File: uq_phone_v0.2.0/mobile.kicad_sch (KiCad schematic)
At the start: 29 parts, among them J10 513382474, J11 513382474, J12 20279-001E-03, J4 20279-001E-03, J5 20279-001E-03, U4 RC7620_1104626

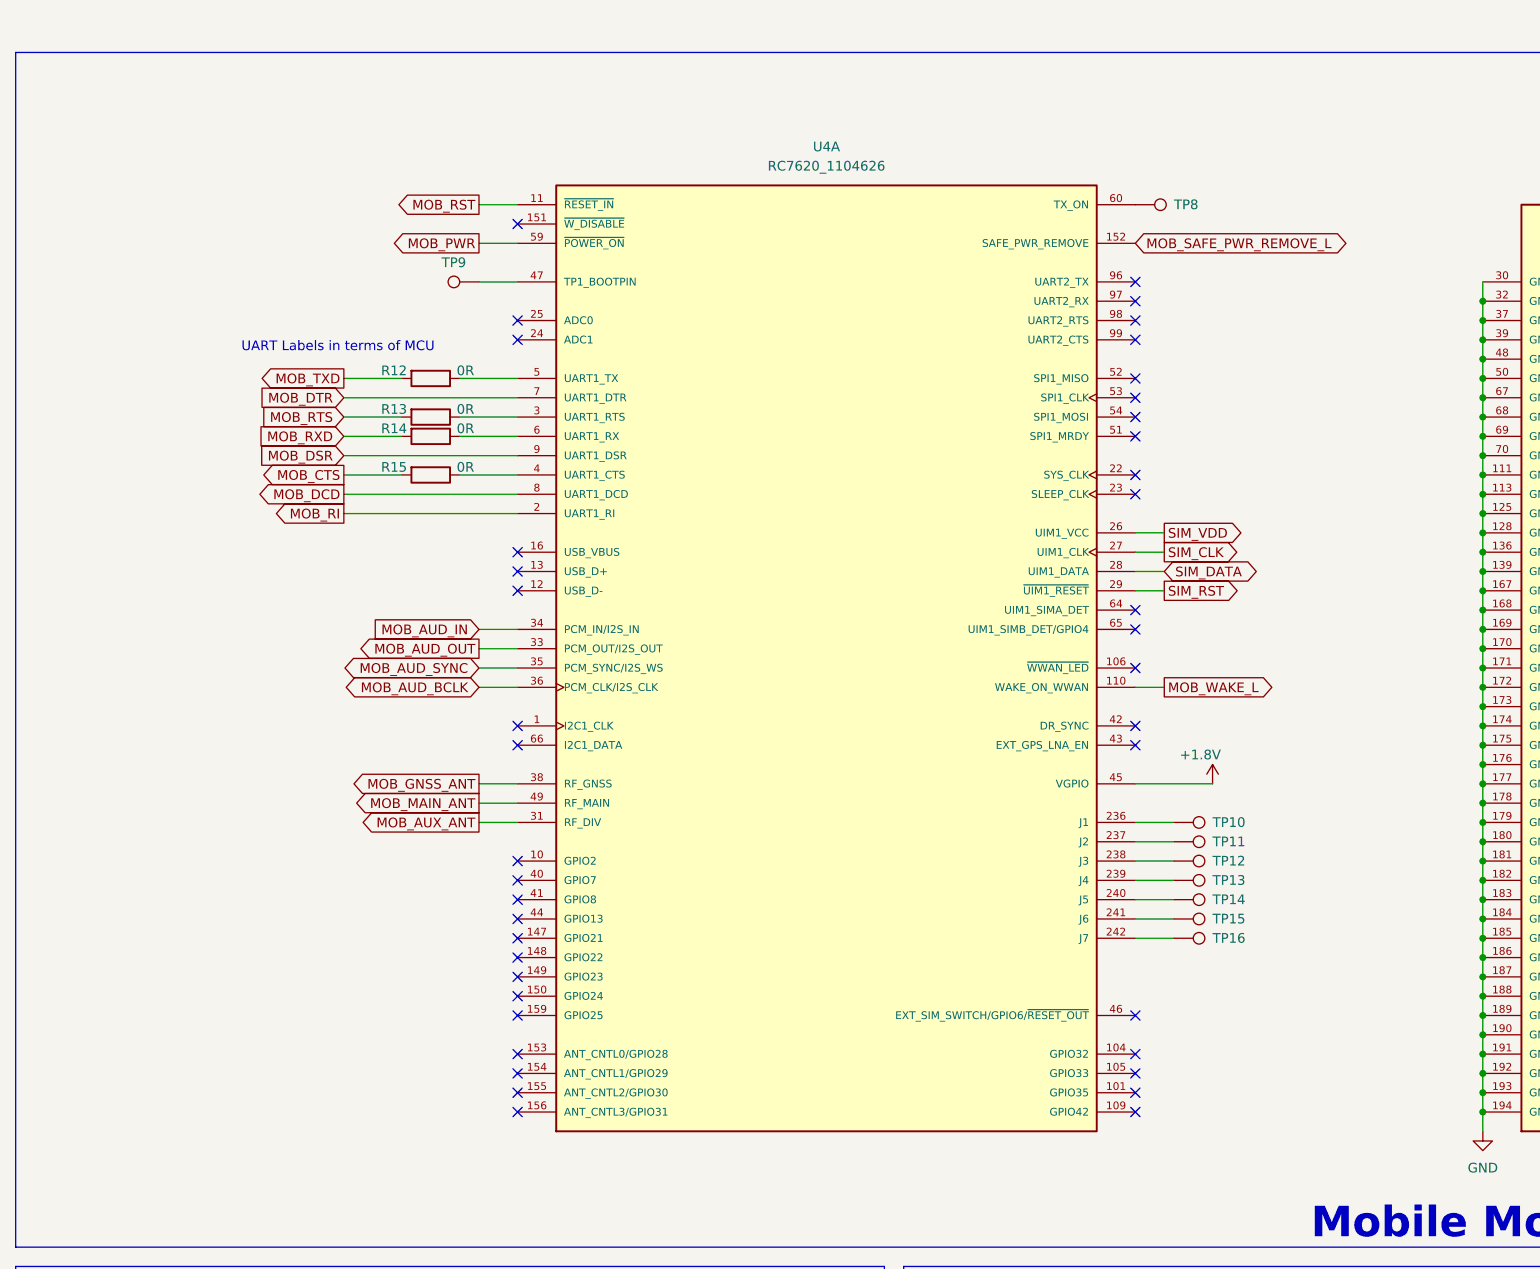
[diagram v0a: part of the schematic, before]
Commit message: Add shared tray detect for MCU and RC7620 SIM detection
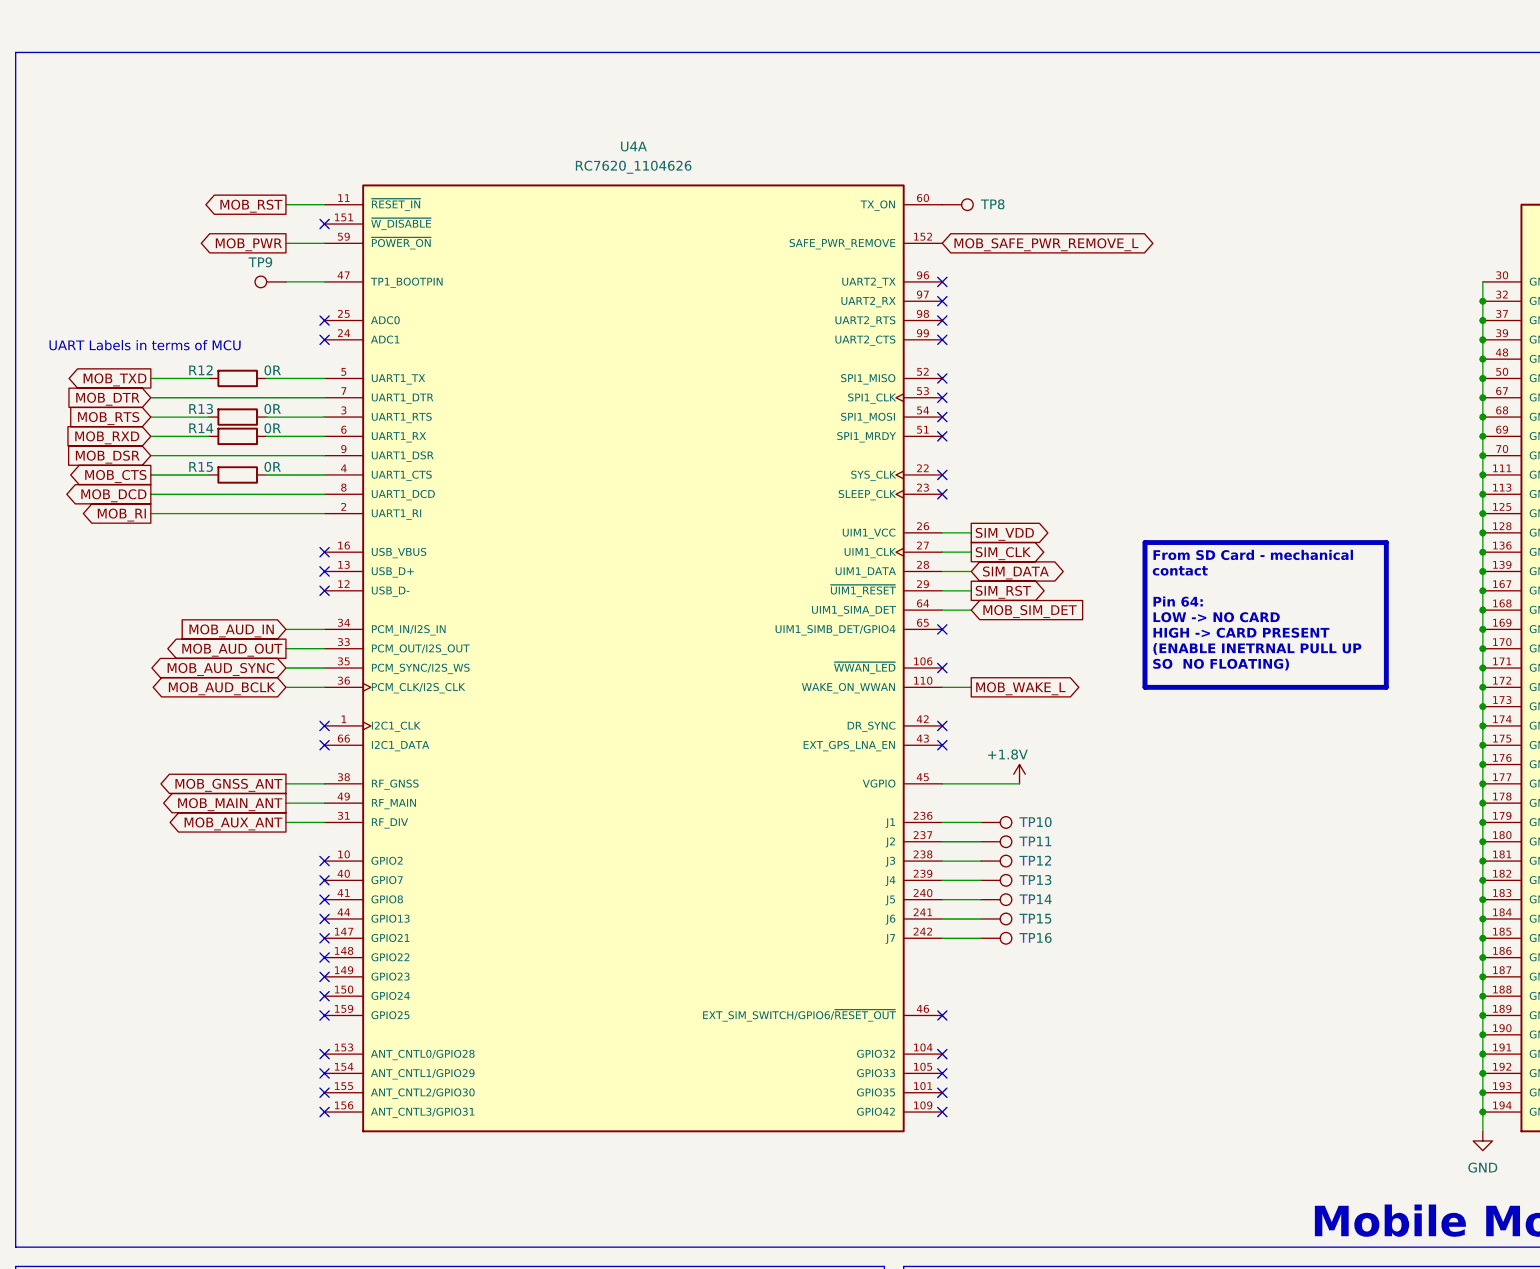
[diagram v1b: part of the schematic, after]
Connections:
- net MOB_SIM_DET: now reaches U4.64 (UIM1_SIMA_DET)
- no-connect marks 41 -> 40
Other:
- moved on the sheet: R12, R13, R14, R15, TP10, TP11, TP12, TP13, TP14, TP15, TP16, TP8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

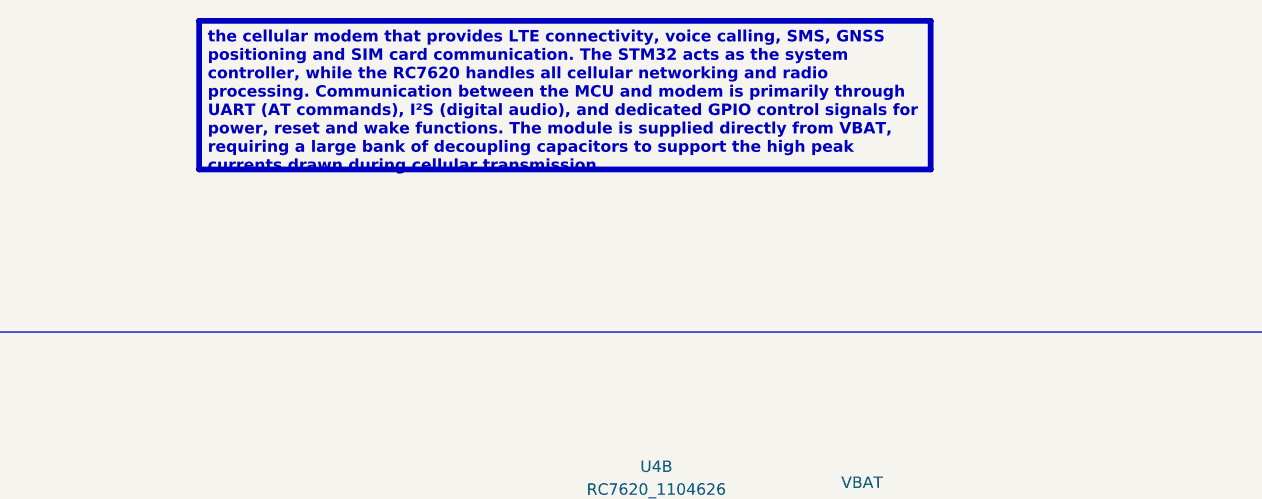
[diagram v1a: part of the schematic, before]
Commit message: Fix KiCad libraries and update soft power circuit
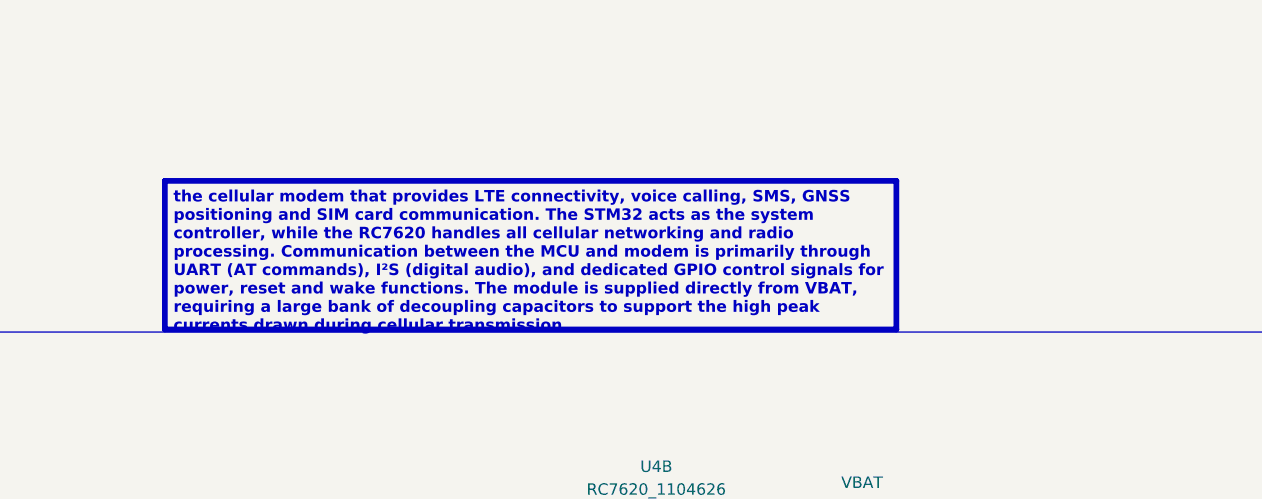
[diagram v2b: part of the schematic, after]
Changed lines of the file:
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@@
 	(text_box "the cellular modem that provides LTE connectivity, voice calling, SMS, GNSS positioning and SIM card communication. The STM32 acts as the system controller, while the RC7620 handles all cellular networking and radio processing. Communication between the MCU and modem is primarily through UART (AT commands), I²S (digital audio), and dedicated GPIO control signals for power, reset and wake functions. The module is supplied directly from VBAT, requiring a large bank of decoupling capacitors to support the high peak currents drawn during cellular transmission."
 		(exclude_from_sim no)
-		(at 179.07 -19.05 0)
+		(at 175.26 -1.27 0)
 		(size 81.28 16.51)
 		(margins 0.9525 0.9525 0.9525 0.9525)

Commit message: Prototype without GPIO expander
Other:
- moved on the sheet: U4C
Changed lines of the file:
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@@
 		(lib_name "RC7620_1104625_1")
 		(lib_id "RC7620_1104625:RC7620_1104625")
-		(at 369.57 35.56 0)
+		(at 361.95 52.07 0)
 		(unit 3)
 		(exclude_from_sim no)
@@
 		(dnp no)
 		(property "Reference" "U4"
-			(at 369.316 28.194 0)
+			(at 361.696 44.704 0)
 			(effects
 				(font
@@
 		)
 		(property "Value" "RC7620_1104626"
-			(at 370.078 30.734 0)
+			(at 362.458 47.244 0)
 			(effects
 				(font
@@
 		)
 		(property "Footprint" "RC7620_1104625:XCVR_RC7620_1104625"
-			(at 369.57 35.56 0)
+			(at 361.95 52.07 0)
 			(effects
 				(font
@@
 		)
 		(property "Datasheet" ""
-			(at 369.57 35.56 0)
+			(at 361.95 52.07 0)
 			(effects
 				(font
@@
 		)
 		(property "Description" ""
-			(at 369.57 35.56 0)
+			(at 361.95 52.07 0)
 			(effects
 				(font
@@
 		)
 		(property "MF" "Sierra Wireless"
-			(at 369.57 35.56 0)
+			(at 361.95 52.07 0)
 			(effects
 				(font
@@
 		)
 		(property "MAXIMUM_PACKAGE_HEIGHT" "2.7mm"
-			(at 369.57 35.56 0)
+			(at 361.95 52.07 0)
 			(effects
 				(font
@@
 		)
 		(property "Package" "BFLGA-239 Sierra Wireless"
-			(at 369.57 35.56 0)
+			(at 361.95 52.07 0)
 			(effects
 				(font
@@
 		)
 		(property "Price" "None"
-			(at 369.57 35.56 0)
+			(at 361.95 52.07 0)
 			(effects
 				(font
@@
 		)
 		(property "Check_prices" "https://www.snapeda.com/parts/RC7620_1104625/Sierra+Wireless/view-part/?ref=eda"
-			(at 369.57 35.56 0)
+			(at 361.95 52.07 0)
 			(effects
 				(font
@@
 		)
 		(property "STANDARD" "Manufacturer Recommendations"
-			(at 369.57 35.56 0)
+			(at 361.95 52.07 0)
 			(effects
 				(font
@@
 		)
 		(property "PARTREV" "12"
-			(at 369.57 35.56 0)
+			(at 361.95 52.07 0)
 			(effects
 				(font
@@
 		)
 		(property "SnapEDA_Link" "https://www.snapeda.com/parts/RC7620_1104625/Sierra+Wireless/view-part/?ref=snap"
-			(at 369.57 35.56 0)
+			(at 361.95 52.07 0)
 			(effects
 				(font
@@
 		)
 		(property "MP" "RC7620_1104625"
-			(at 369.57 35.56 0)
+			(at 361.95 52.07 0)
 			(effects
 				(font
@@
 		)
 		(property "Description_1" "\n                        \n                            Cellular, Navigation 2G, 3G, 4G, EDGE, GPRS, GSM, LTE, UMTS Transceiver Module 900MHz, 1.8GHz Antenna Not Included Surface Mount\n                        \n"
-			(at 369.57 35.56 0)
+			(at 361.95 52.07 0)
 			(effects
 				(font
@@
 		)
 		(property "MANUFACTURER" "Sierra Wireless"
-			(at 369.57 35.56 0)
+			(at 361.95 52.07 0)
 			(effects
 				(font
@@
 		)
 		(property "Availability" "In Stock"
-			(at 369.57 35.56 0)
+			(at 361.95 52.07 0)
 			(effects
 				(font
@@
 		)
 		(property "SNAPEDA_PN" "RC7620_1104625"
-			(at 369.57 35.56 0)
+			(at 361.95 52.07 0)
 			(effects
 				(font
@@
 		)
 		(property "DESCRIPTION" ""
-			(at 369.57 35.56 0)
+			(at 361.95 52.07 0)
 			(effects
 				(font
@@
 		)
 		(property "LSCS PN" ""
-			(at 369.57 35.56 0)
+			(at 361.95 52.07 0)
 			(effects
 				(font
